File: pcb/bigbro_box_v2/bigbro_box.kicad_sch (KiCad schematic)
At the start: 49 parts, among them J1 CT_AMP, J2 Display, J3 Mains, J4 UART flashing, J5 Conn_01x02, J6 Relay, K1 G5LE-1, Q1 MMBT3904, Q2 MMBT3904, Q3 BSS138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

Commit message: Optimize allocation of gates.
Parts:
- removed SW1: SW_SPDT, Connector_JST:JST_XH_B3B-XH-A_1x03_P2.50mm_Vertical, symbol Switch:SW_SPDT
- added SW1: SW_SPST, Connector_JST:JST_XH_B2B-XH-A_1x02_P2.50mm_Vertical, symbol Switch:SW_SPST
- Q3: footprint Package_TO_SOT_SMD:SOT-323_SC-70_Handsoldering -> Package_TO_SOT_SMD:SOT-323_SC-70
- R1, R2, R3, R4, R5, R7, R8: footprint Resistor_SMD:R_0603_1608Metric_Pad0.98x0.95mm_HandSolder -> Resistor_SMD:R_0603_1608Metric
- renumbered U4 to U3, U3 to U4
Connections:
- net +3V3: now also U3.12, U3.13, SW1.2 (B); no longer U3.5, U3.6
- net GND: now also U4.5, U4.6; no longer U4.1, U4.2
- net Relay_reset: now also U4.11; no longer U4.10
- net Relay_trig: now also U3.8, U4.10; no longer U3.1, U4.11
- net card_switch: now also U3.1, U3.2, U4.8, SW1.1 (A); no longer U3.8, U3.9, U4.12
- net relay: now also U3.10; no longer U3.3
- net relay_gpio: now also U4.1, U4.2, U4.9; no longer U4.12, U4.13, U4.13
- net ~{card_switch}: now also U4.13, U4.3; no longer U4.11, U4.9
- net ~{relay_gpio}: now also U3.3, U4.12; no longer U3.10, U4.8
- net at U3.4: now also U3.9; no longer U3.2
- no-connect marks 13 -> 12
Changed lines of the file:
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@@
   (no_connect (at 58.42 72.39))
   (no_connect (at 88.9 67.31))
-  (no_connect (at 133.35 97.79))
   (no_connect (at 127 173.99))
   (no_connect (at 88.9 74.93))
@@
     (stroke (width 0) (type default))
   )
-  (wire (pts (xy 133.35 92.71) (xy 130.81 92.71))
+  (wire (pts (xy 133.35 95.25) (xy 130.81 95.25))
     (stroke (width 0) (type default))
   )
@@
     (effects (font (size 1.27 1.27)) (justify left))
   )
-  (hierarchical_label "card_switch" (shape output) (at 130.81 92.71 180) (fields_autoplaced)
+  (hierarchical_label "card_switch" (shape output) (at 130.81 95.25 180) (fields_autoplaced)
     (effects (font (size 1.27 1.27)) (justify right))
   )
@@
       (effects (font (size 1.27 1.27)) (justify left))
     )
-    (property "Footprint" "Resistor_SMD:R_0603_1608Metric_Pad0.98x0.95mm_HandSolder" (at 325.12 105.41 0)
+    (property "Footprint" "Resistor_SMD:R_0603_1608Metric" (at 325.12 105.41 0)
       (effects (font (size 1.27 1.27)) hide)
     )
@@
       (effects (font (size 1.27 1.27)) (justify left))
     )
-    (property "Footprint" "Package_TO_SOT_SMD:SOT-323_SC-70_Handsoldering" (at 344.17 99.06 0)
+    (property "Footprint" "Package_TO_SOT_SMD:SOT-323_SC-70" (at 344.17 99.06 0)
       (effects (font (size 1.27 1.27)) hide)
     )
@@
       (effects (font (size 1.27 1.27)) (justify right))
     )
-    (property "Footprint" "Resistor_SMD:R_0603_1608Metric_Pad0.98x0.95mm_HandSolder" (at 76.2 167.64 0)
+    (property "Footprint" "Resistor_SMD:R_0603_1608Metric" (at 76.2 167.64 0)
       (effects (font (size 1.27 1.27)) hide)
     )
@@
     )
   )
-  (symbol (lib_id "Switch:SW_SPDT") (at 138.43 95.25 180) (unit 1)
-    (in_bom yes) (on_board yes) (dnp no)
-    (property "Reference" "SW1" (at 138.43 87.63 0)
-      (effects (font (size 1.27 1.27)))
-    )
-    (property "Value" "SW_SPDT" (at 138.43 90.17 0)
-      (effects (font (size 1.27 1.27)))
-    )
-    (property "Footprint" "Connector_JST:JST_XH_B3B-XH-A_1x03_P2.50mm_Vertical" (at 138.43 95.25 0)
-      (effects (font (size 1.27 1.27)) hide)
-    )
-    (property "Datasheet" "~" (at 138.43 95.25 0)
-      (effects (font (size 1.27 1.27)) hide)
-    )
-    (pin "1")
-    (pin "2")
-    (pin "3")
-    (instances
-      (project "bigbro_box"
-        (path "/212a0d71-cc7b-49f8-b4ca-a935e5355dca"
-          (reference "SW1") (unit 1)
-        )
-      )
-    )
-  )
   (symbol (lib_id "power:+5V") (at 341.63 71.12 0) (unit 1)
     (in_bom yes) (on_board yes) (dnp no) (fields_autoplaced)
@@
       (effects (font (size 1.27 1.27)) (justify right))
     )
-    (property "Footprint" "Resistor_SMD:R_0603_1608Metric_Pad0.98x0.95mm_HandSolder" (at 165.1 85.09 0)
+    (property "Footprint" "Resistor_SMD:R_0603_1608Metric" (at 165.1 85.09 0)
       (effects (font (size 1.27 1.27)) hide)
     )
@@
       (effects (font (size 1.27 1.27)) (justify right))
     )
-    (property "Footprint" "Resistor_SMD:R_0603_1608Metric_Pad0.98x0.95mm_HandSolder" (at 68.58 175.26 0)
+    (property "Footprint" "Resistor_SMD:R_0603_1608Metric" (at 68.58 175.26 0)
       (effects (font (size 1.27 1.27)) hide)
     )
@@
     )
   )
-  (symbol (lib_id "4xxx:4011") (at 147.32 173.99 0) (unit 2)
+  (symbol (lib_id "4xxx:4011") (at 147.32 173.99 0) (unit 4)
     (in_bom yes) (on_board yes) (dnp no) (fields_autoplaced)
-    (property "Reference" "U4" (at 147.3117 166.37 0)
+    (property "Reference" "U3" (at 147.3117 166.37 0)
       (effects (font (size 1.27 1.27)))
     )
@@
       (project "bigbro_box"
         (path "/212a0d71-cc7b-49f8-b4ca-a935e5355dca"
-          (reference "U4") (unit 2)
+          (reference "U3") (unit 4)
         )
       )
@@
     )
   )
-  (symbol (lib_id "4xxx:4011") (at 59.69 142.24 0) (unit 3)
+  (symbol (lib_id "4xxx:4011") (at 59.69 142.24 0) (unit 1)
     (in_bom yes) (on_board yes) (dnp no)
-    (property "Reference" "U4" (at 44.45 140.97 0)
+    (property "Reference" "U3" (at 44.45 140.97 0)
       (effects (font (size 1.27 1.27)))
     )
@@
       (project "bigbro_box"
         (path "/212a0d71-cc7b-49f8-b4ca-a935e5355dca"
-          (reference "U4") (unit 3)
+          (reference "U3") (unit 1)
         )
       )
@@
     )
   )
-  (symbol (lib_id "4xxx:4011") (at 119.38 173.99 0) (unit 1)
+  (symbol (lib_id "4xxx:4011") (at 119.38 173.99 0) (unit 2)
     (in_bom yes) (on_board yes) (dnp no) (fields_autoplaced)
     (property "Reference" "U4" (at 119.3717 166.37 0)
@@
       (project "bigbro_box"
         (path "/212a0d71-cc7b-49f8-b4ca-a935e5355dca"
-          (reference "U4") (unit 1)
+          (reference "U4") (unit 2)
         )
       )
@@
       (effects (font (size 1.27 1.27)))
     )
-    (property "Footprint" "Resistor_SMD:R_0603_1608Metric_Pad0.98x0.95mm_HandSolder" (at 328.93 101.6 0)
+    (property "Footprint" "Resistor_SMD:R_0603_1608Metric" (at 328.93 101.6 0)
       (effects (font (size 1.27 1.27)) hide)
     )
@@
       (effects (font (size 1.27 1.27)) (justify left))
     )
-    (property "Footprint" "Resistor_SMD:R_0603_1608Metric_Pad0.98x0.95mm_HandSolder" (at 35.56 130.81 0)
+    (property "Footprint" "Resistor_SMD:R_0603_1608Metric" (at 35.56 130.81 0)
       (effects (font (size 1.27 1.27)) hide)
     )
@@
     )
   )
-  (symbol (lib_id "4xxx:4011") (at 59.69 151.13 0) (unit 4)
+  (symbol (lib_id "4xxx:4011") (at 59.69 151.13 0) (unit 1)
     (in_bom yes) (on_board yes) (dnp no)
     (property "Reference" "U4" (at 44.45 149.86 0)
@@
       (project "bigbro_box"
         (path "/212a0d71-cc7b-49f8-b4ca-a935e5355dca"
-          (reference "U4") (unit 4)
+          (reference "U4") (unit 1)
         )
       )
     )
   )
-  (symbol (lib_id "4xxx:4011") (at 87.63 144.78 0) (unit 3)
+  (symbol (lib_id "4xxx:4011") (at 87.63 144.78 0) (unit 4)
     (in_bom yes) (on_board yes) (dnp no)
-    (property "Reference" "U3" (at 87.63 149.86 0)
+    (property "Reference" "U4" (at 87.63 149.86 0)
       (effects (font (size 1.27 1.27)))
     )
@@
       (project "bigbro_box"
         (path "/212a0d71-cc7b-49f8-b4ca-a935e5355dca"
-          (reference "U3") (unit 3)
+          (reference "U4") (unit 4)
         )
       )
@@
     )
   )
-  (symbol (lib_id "4xxx:4011") (at 87.63 124.46 0) (unit 4)
+  (symbol (lib_id "4xxx:4011") (at 87.63 124.46 0) (unit 3)
     (in_bom yes) (on_board yes) (dnp no)
-    (property "Reference" "U3" (at 87.63 116.84 0)
+    (property "Reference" "U4" (at 87.63 116.84 0)
       (effects (font (size 1.27 1.27)))
     )
@@
       (project "bigbro_box"
         (path "/212a0d71-cc7b-49f8-b4ca-a935e5355dca"
-          (reference "U3") (unit 4)
+          (reference "U4") (unit 3)
         )
       )
@@
       (effects (font (size 1.27 1.27)) (justify right))
     )
-    (property "Footprint" "Resistor_SMD:R_0603_1608Metric_Pad0.98x0.95mm_HandSolder" (at 165.1 92.71 0)
+    (property "Footprint" "Resistor_SMD:R_0603_1608Metric" (at 165.1 92.71 0)
       (effects (font (size 1.27 1.27)) hide)
     )
@@
     )
   )
-  (symbol (lib_id "4xxx:4011") (at 119.38 127 0) (unit 1)
+  (symbol (lib_id "4xxx:4011") (at 119.38 127 0) (unit 3)
     (in_bom yes) (on_board yes) (dnp no) (fields_autoplaced)
     (property "Reference" "U3" (at 119.38 118.11 0)
@@
       (project "bigbro_box"
         (path "/212a0d71-cc7b-49f8-b4ca-a935e5355dca"
-          (reference "U3") (unit 1)
+          (reference "U3") (unit 3)
         )
       )
@@
         )
       )
+    )
+  )
+  (symbol (lib_id "Switch:SW_SPST") (at 138.43 95.25 0) (unit 1)
+    (in_bom yes) (on_board yes) (dnp no) (fields_autoplaced)
+    (property "Reference" "SW1" (at 138.43 90.17 0)
+      (effects (font (size 1.27 1.27)))
+    )
+    (property "Value" "SW_SPST" (at 138.43 92.71 0)
+      (effects (font (size 1.27 1.27)))
+    )
+    (property "Footprint" "Connector_JST:JST_XH_B2B-XH-A_1x02_P2.50mm_Vertical" (at 138.43 95.25 0)
+      (effects (font (size 1.27 1.27)) hide)
+    )
+    (property "Datasheet" "~" (at 138.43 95.25 0)
+      (effects (font (size 1.27 1.27)) hide)
+    )
+    (pin "1")
+    (pin "2")
+    (instances
+      (project "bigbro_box"
+        (path "/212a0d71-cc7b-49f8-b4ca-a935e5355dca"
+          (reference "SW1") (unit 1)
+        )
+      )

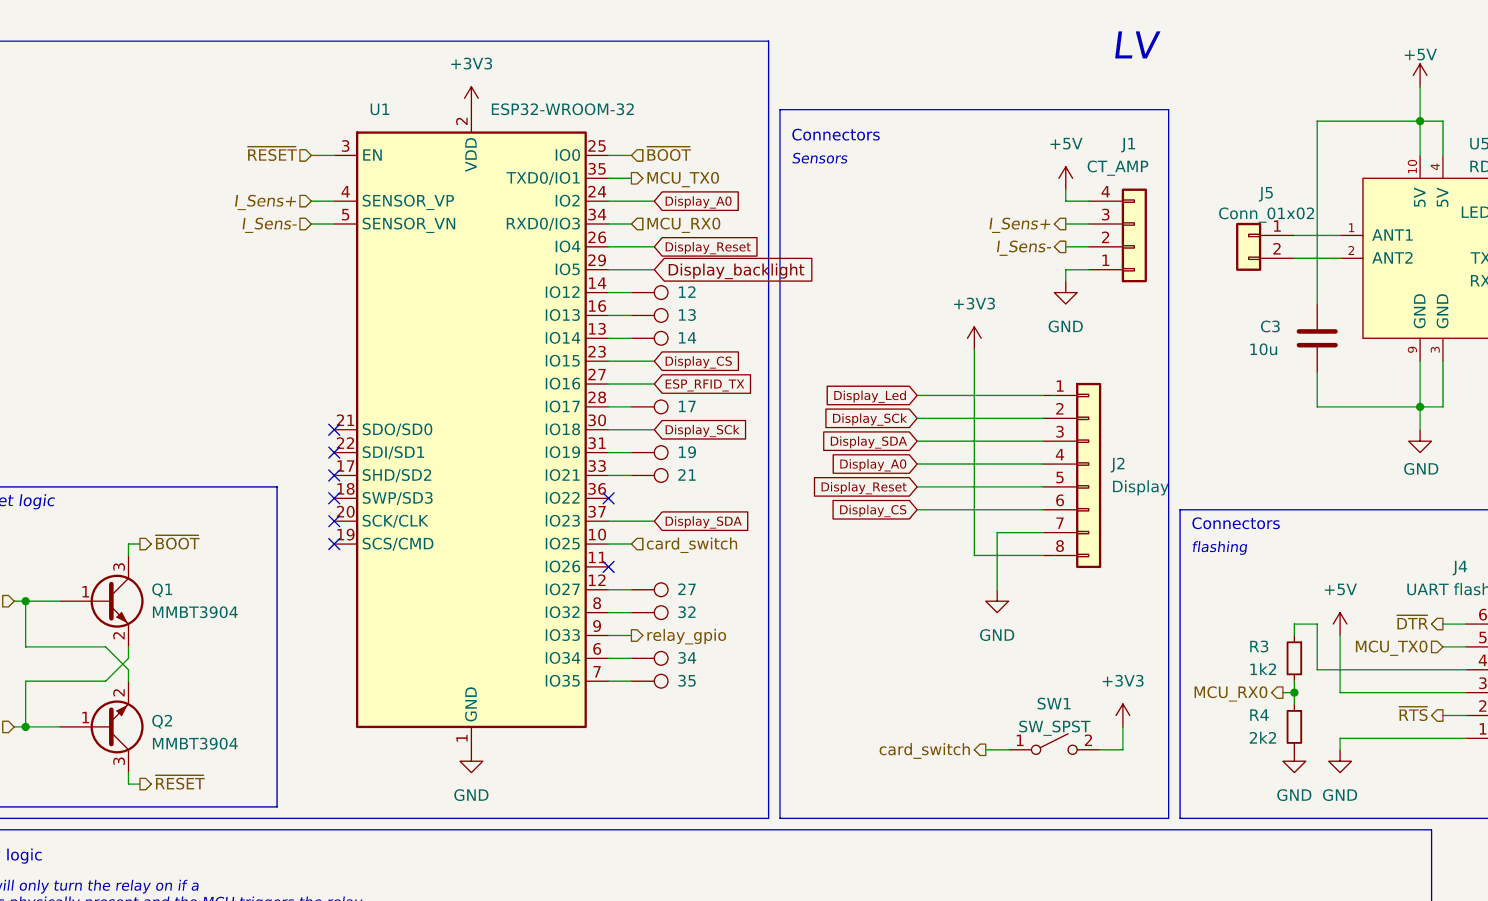
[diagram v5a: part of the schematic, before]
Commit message: Change current sense to single pin.
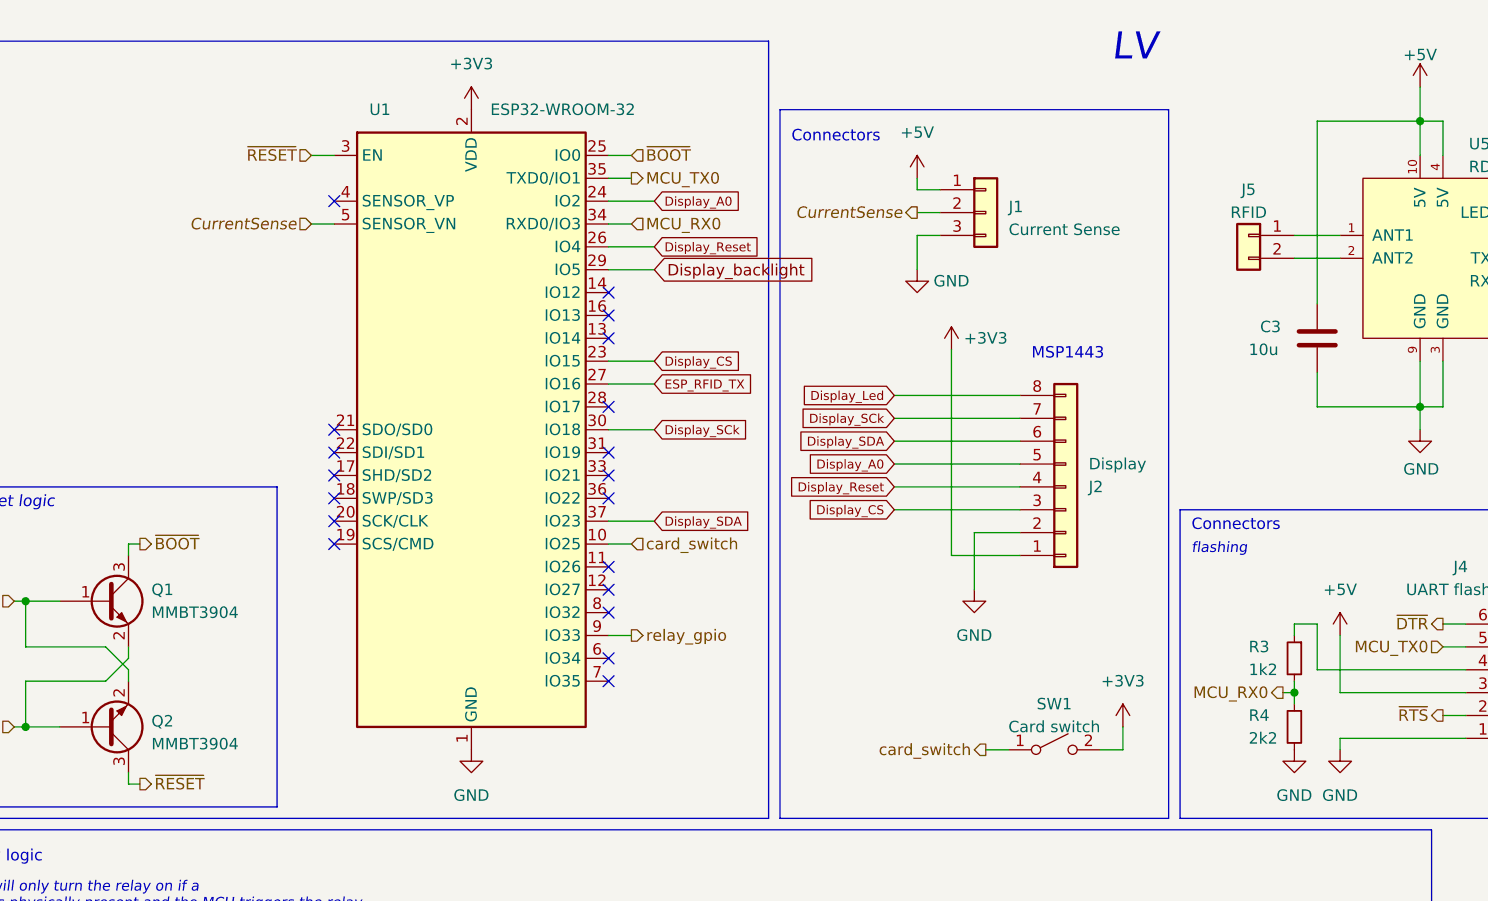
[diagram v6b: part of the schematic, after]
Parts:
- removed J1: CT_AMP, Connector_JST:JST_XH_B4B-XH-A_1x04_P2.50mm_Vertical, symbol Connector_Generic:Conn_01x04
- removed TP1: 12, TestPoint:TestPoint_Pad_D1.0mm, symbol Connector:TestPoint
- removed TP10: 35, TestPoint:TestPoint_Pad_D1.0mm, symbol Connector:TestPoint
- removed TP2: 13, TestPoint:TestPoint_Pad_D1.0mm, symbol Connector:TestPoint
- removed TP3: 14, TestPoint:TestPoint_Pad_D1.0mm, symbol Connector:TestPoint
- removed TP4: 17, TestPoint:TestPoint_Pad_D1.0mm, symbol Connector:TestPoint
- removed TP5: 19, TestPoint:TestPoint_Pad_D1.0mm, symbol Connector:TestPoint
- removed TP6: 21, TestPoint:TestPoint_Pad_D1.0mm, symbol Connector:TestPoint
- removed TP7: 27, TestPoint:TestPoint_Pad_D1.0mm, symbol Connector:TestPoint
- removed TP8: 32, TestPoint:TestPoint_Pad_D1.0mm, symbol Connector:TestPoint
- removed TP9: 34, TestPoint:TestPoint_Pad_D1.0mm, symbol Connector:TestPoint
- added J1: Current Sense, Connector_JST:JST_XH_B3B-XH-A_1x03_P2.50mm_Vertical, symbol Connector_Generic:Conn_01x03
- J5: value Conn_01x02 -> RFID
- SW1: value SW_SPST -> Card switch
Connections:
- net +3V3: now also J2.1 (Pin_1); no longer J2.8 (Pin_8)
- net +5V: now also J1.1 (Pin_1)
- net Display_A0: now also J2.5 (Pin_5); no longer J2.4 (Pin_4)
- net Display_CS: now also J2.3 (Pin_3); no longer J2.6 (Pin_6)
- net Display_Led: now also J2.8 (Pin_8); no longer J2.1 (Pin_1)
- net Display_Reset: now also J2.4 (Pin_4); no longer J2.5 (Pin_5)
- net Display_SCk: now also J2.7 (Pin_7); no longer J2.2 (Pin_2)
- net Display_SDA: now also J2.6 (Pin_6); no longer J2.3 (Pin_3)
- net GND: now also J2.2 (Pin_2), J1.3 (Pin_3); no longer J2.7 (Pin_7)
- net I_Sens+: no longer names the net of U1.4 (SENSOR_VP)
- net I_Sens- renamed CurrentSense
- net CurrentSense: now also J1.2 (Pin_2)
- no-connect marks 12 -> 23
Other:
- note added: "MSP1443"
- note removed: "Sensors"
- moved on the sheet: J2

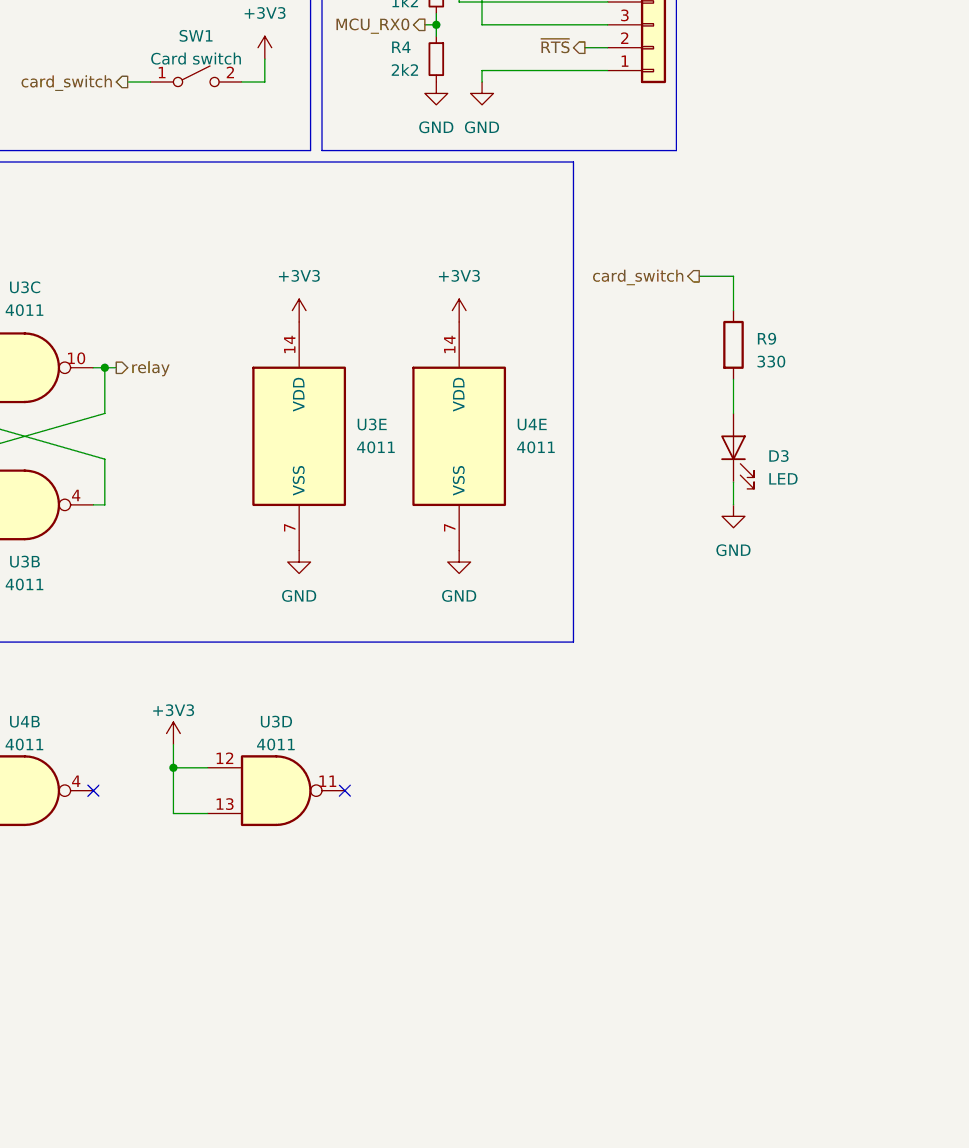
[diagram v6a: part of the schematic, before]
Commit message: Route flip-flop, reduce width to 100 mm.
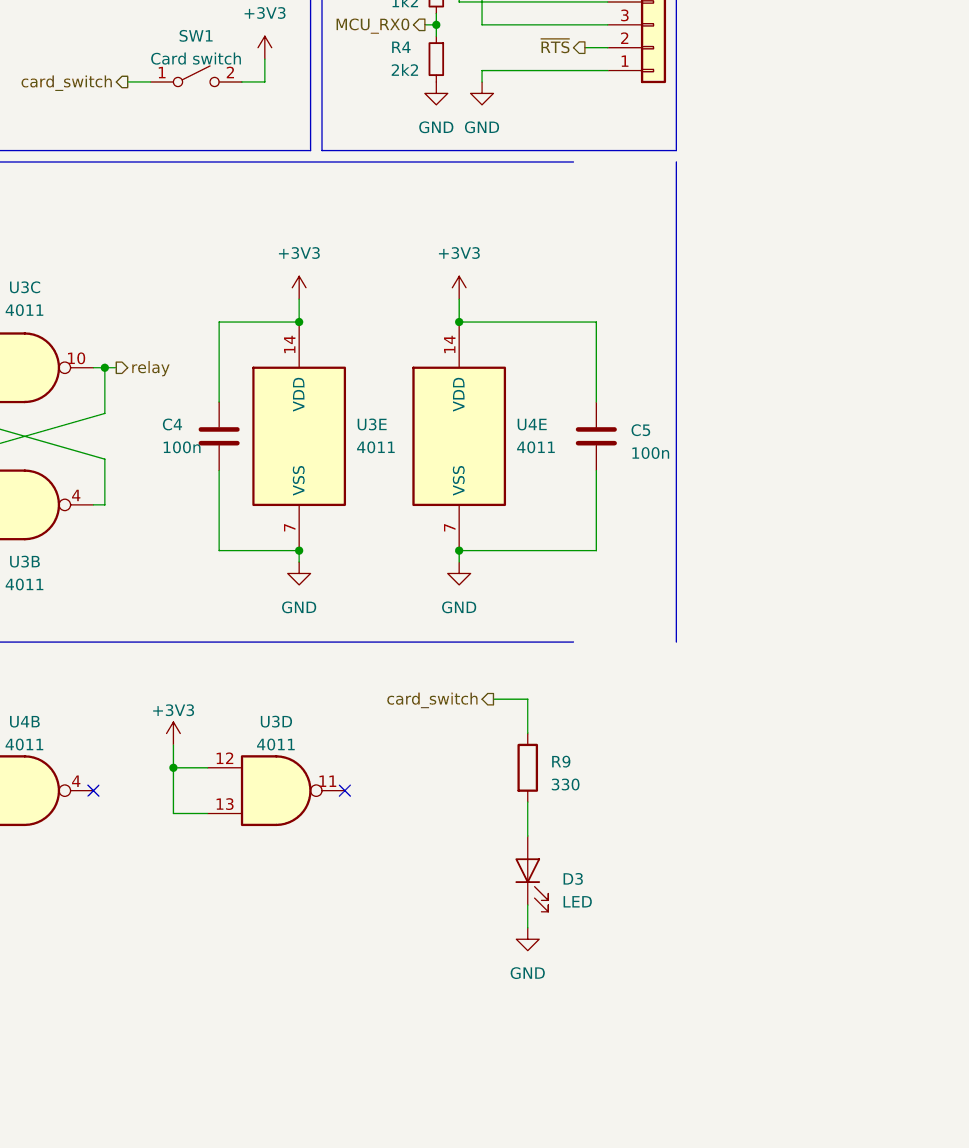
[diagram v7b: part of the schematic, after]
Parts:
- added C4, C5: 100n, Capacitor_SMD:C_0603_1608Metric, symbol Device:C
- C1: footprint Capacitor_SMD:C_0603_1608Metric_Pad1.08x0.95mm_HandSolder -> Capacitor_SMD:C_0603_1608Metric
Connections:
- net +3V3: now also C4.1, C5.1
- net GND: now also C4.2, C5.2
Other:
- moved on the sheet: D3, R9
